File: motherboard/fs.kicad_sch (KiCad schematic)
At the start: 69 parts, among them J101 SC10L, J102 640389-2, Q101 MJD44H11, Q102 MJD45H11, U101 INA132UA, U102 LM741C, U103 LMH6609, U104 LM317, U105 LM337, U106 LM340-5, U107 MC7905ACD2T

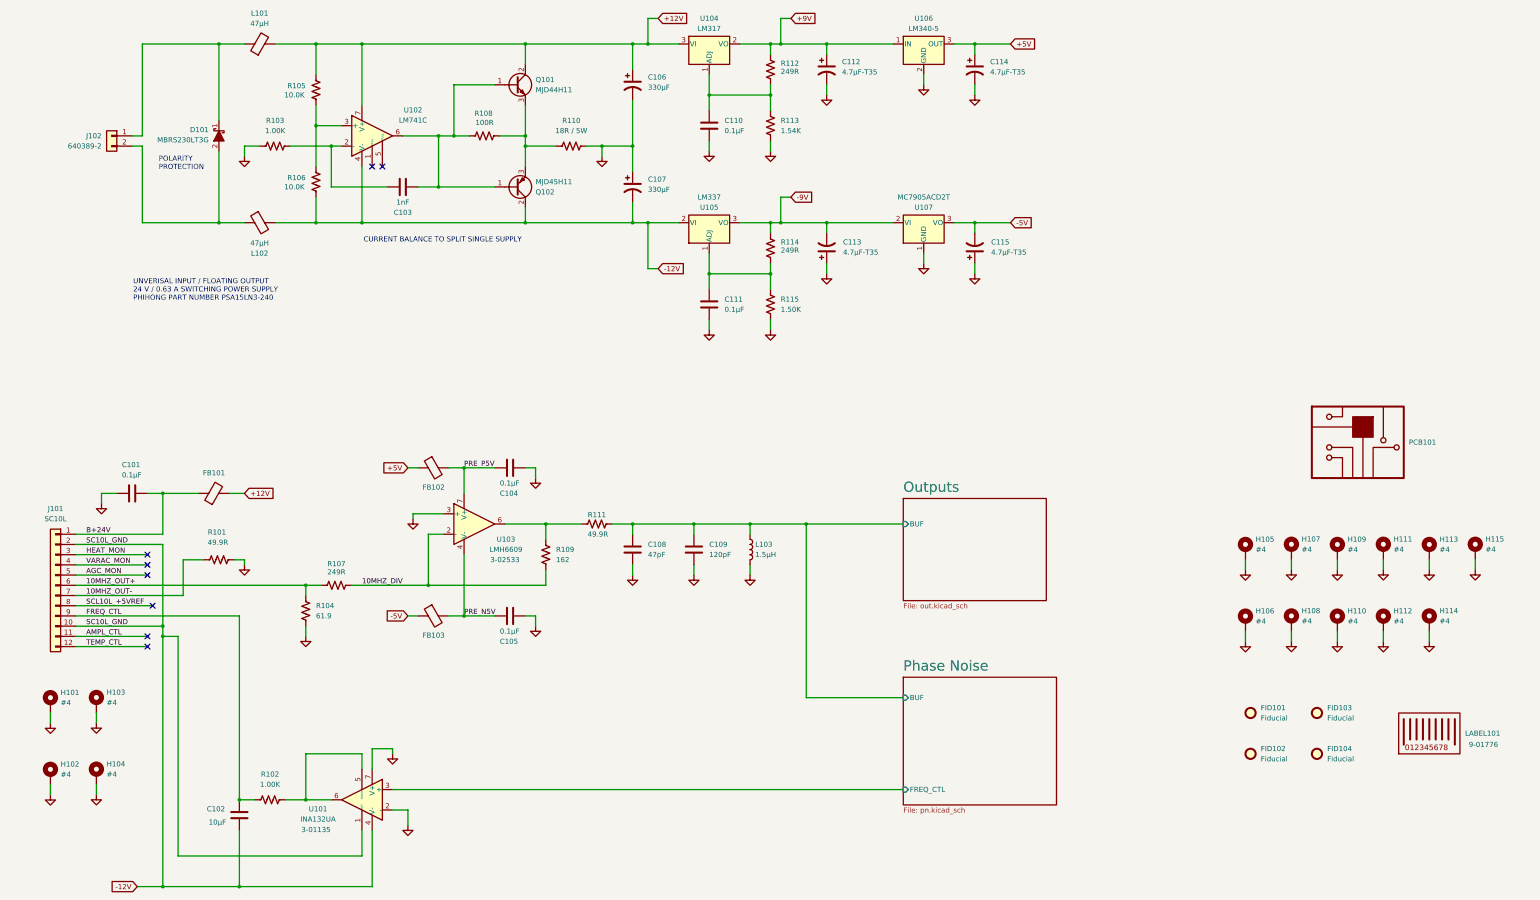
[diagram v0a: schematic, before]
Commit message: fix ERC issues
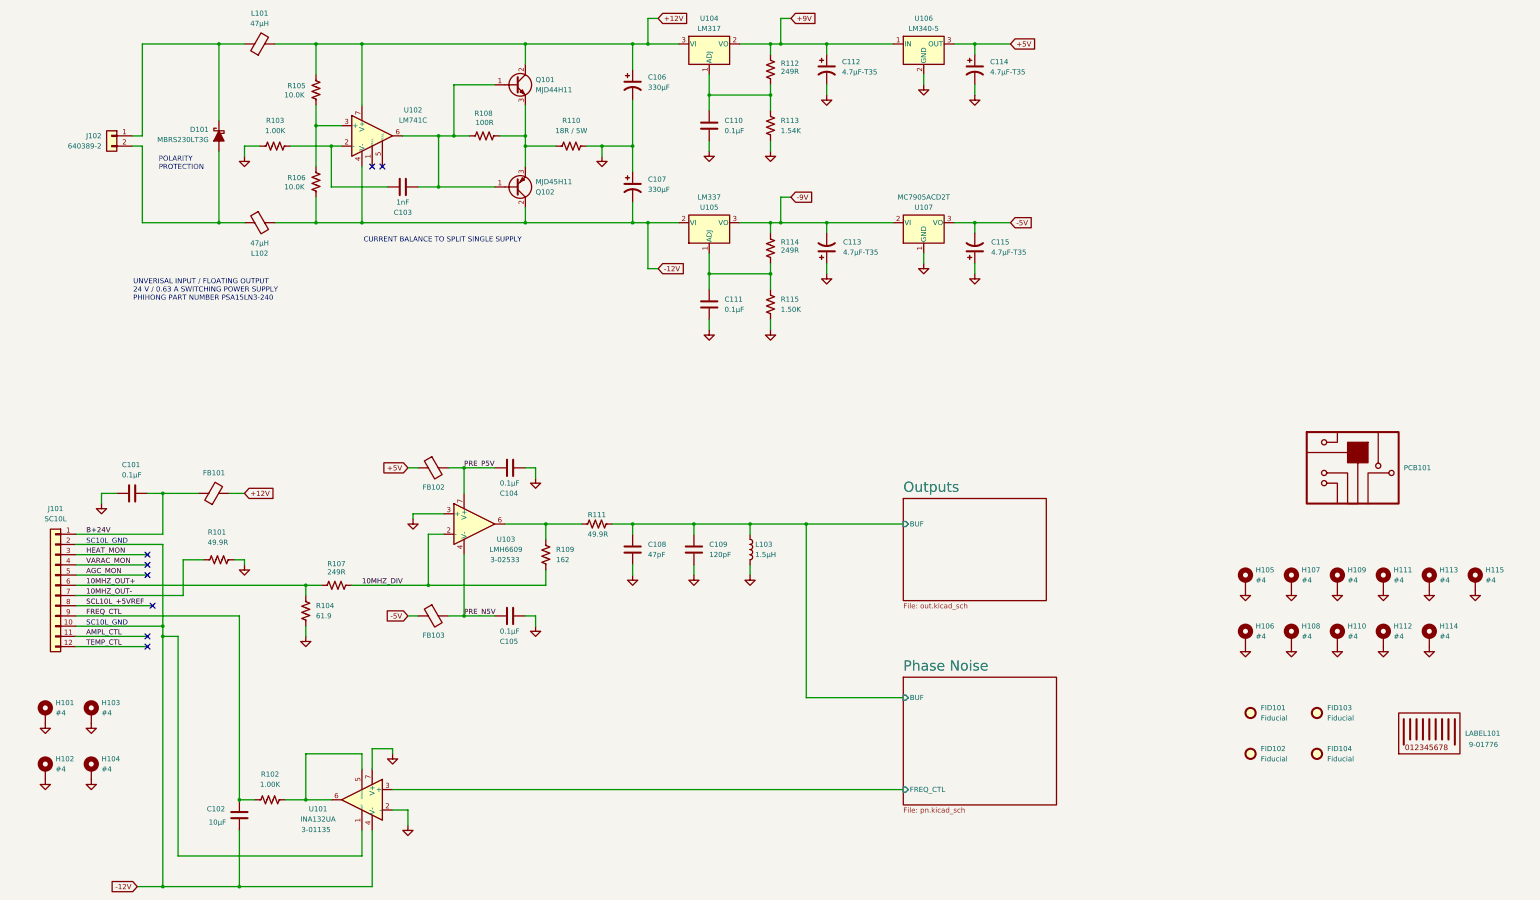
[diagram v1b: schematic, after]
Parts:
- removed D101: MBRS230LT3G, Diode_SMD:D_SMB, symbol SRS diodes:Schottky/MBRS230LT3G 2A 30V
- added D101: MBRS230LT3G, Diode_SMD:D_SMB, symbol #SRS:3_ICs/3-02091
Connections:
- net at J102.1 (Pin_1), L101.1: now also D101.1 (K)
- net at J102.2 (Pin_2), L102.1: now also D101.2 (A)
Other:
- note added: "SC10L_GND"
- moved on the sheet: H101, H102, H103, H104, H105, H106, H107, H108, H109, H110, H111, H112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

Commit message: add ESD protection (14V TVS)
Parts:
- C103: value 1nF -> 1nF NP0
- R104: value 61.9 -> 61.9R
- R109: value 162 -> 162R
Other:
- note added: "UNIVERSAL INPUT / FLOATING OUTPUT 24 V / 0.63 A SWITCHING POWER SUPPLY PHIHONG PART NUMBER PSA15LN3-240"
- note removed: "UNVERISAL INPUT / FLOATING OUTPUT 24 V / 0.63 A SWITCHING POWER SUPPLY PHIHONG PART NUMBER PSA15LN3-240"
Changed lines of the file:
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@@
 		)
 	)
-	(text "UNVERISAL INPUT / FLOATING OUTPUT\n24 V / 0.63 A SWITCHING POWER SUPPLY\nPHIHONG PART NUMBER PSA15LN3-240"
+	(text "UNIVERSAL INPUT / FLOATING OUTPUT\n24 V / 0.63 A SWITCHING POWER SUPPLY\nPHIHONG PART NUMBER PSA15LN3-240"
 		(exclude_from_sim no)
 		(at 57.404 100.584 0)
@@
 			)
 		)
-		(property "Value" "61.9"
+		(property "Value" "61.9R"
 			(at 102.87 181.6099 0)
 			(show_name no)
@@
 			)
 		)
-		(property "Value" "162"
+		(property "Value" "162R"
 			(at 162.56 167.6399 0)
 			(show_name no)
@@
 			)
 		)
-		(property "Value" "1nF"
+		(property "Value" "1nF NP0"
 			(at 124.46 78.74 90)
 			(show_name no)

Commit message: add mechanical parts to bom
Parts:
- J101: value SC10L -> Header; JLCPCB -- -> C7155422; MPN -- -> 1-215299-2; SRS PN -- -> 1-01602
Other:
- note added: "FEMALE HEADER TO SC10L ADAPTER BOARD"
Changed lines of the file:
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@@
 		)
 	)
+	(text "FEMALE HEADER TO SC10L\nADAPTER BOARD"
+		(exclude_from_sim no)
+		(at 40.64 194.564 0)
+		(effects
+			(font
+				(size 1.27 1.27)
+			)
+		)
+	)
 	(text "CURRENT BALANCE TO SPLIT SINGLE SUPPLY"
 		(exclude_from_sim no)
@@
 		(in_pos_files yes)
 		(dnp no)
-		(fields_autoplaced yes)
 		(property "Reference" "J101"
 			(at 38.1 154.94 0)
@@
 			)
 		)
-		(property "Value" "SC10L"
+		(property "Value" "Header"
 			(at 38.1 157.48 0)
+			(hide yes)
 			(show_name no)
 			(do_not_autoplace no)
@@
 			)
 		)
-		(property "JLCPCB" "--"
+		(property "JLCPCB" "C7155422"
 			(at 38.1 173.99 0)
 			(hide yes)
@@
 			)
 		)
-		(property "MPN" "--"
+		(property "MPN" "1-215299-2"
 			(at 38.1 173.99 0)
 			(hide yes)
@@
 			)
 		)
-		(property "SRS PN" "--"
-			(at 38.1 173.99 0)
-			(hide yes)
+		(property "SRS PN" "1-01602"
+			(at 38.1 157.988 0)
 			(show_name no)
 			(do_not_autoplace no)

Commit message: add schematic annotations
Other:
- note added: "ESTIMATED MAX CURRENT DRAW ========================== RAIL CURRENT POWER NOTES +12 V 0.52 A 6.24 W OCXO PLUS ALL POSITIVE-RAIL LOADS −12 V 0.52 A 6.24 W RETURN CURRENT OF THE FLOATING 24 V SUPPLY +9 V 0.31 A 2.79 W +5 V REG PLUS +9 V LOADS −9 V 0.24 A 2.16 W −5 V REG PLUS −9 V LOADS +5 V 0.21 A 1.05 W 8x LMH6609S PLUS SIX GROUNDED OUTPUTS −5 V 0.20 A 1.00 W 8x LMH6609S PLUS SIX GROUNDED OUTPUTS A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"
- note added: "UNIVERSAL INPUT / FLOATING OUTPUT 24 V / 1.50 A SWITCHING POWER SUPPLY MEANWELL PART NUMBER EPS-35-24"
- note removed: "UNIVERSAL INPUT / FLOATING OUTPUT 24 V / 0.63 A SWITCHING POWER SUPPLY PHIHONG PART NUMBER PSA15LN3-240"
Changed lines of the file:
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@@
+		)
+	)
+	(text "ESTIMATED MAX CURRENT DRAW\n==========================\n\nRAIL	CURRENT	POWER	NOTES\n+12 V	0.52 A	6.24 W	OCXO PLUS ALL POSITIVE-RAIL LOADS\n−12 V	0.52 A	6.24 W	RETURN CURRENT OF THE FLOATING 24 V SUPPLY\n+9 V	0.31 A	2.79 W	+5 V REG PLUS +9 V LOADS\n−9 V	0.24 A	2.16 W	−5 V REG PLUS −9 V LOADS\n+5 V	0.21 A	1.05 W	8x LMH6609S PLUS SIX GROUNDED OUTPUTS\n−5 V	0.20 A	1.00 W	8x LMH6609S PLUS SIX GROUNDED OUTPUTS\n\nASSUMPTIONS:\n\n	- SC-10L STABLE AT 25 °C\n	- ALL SIX OUTPUTS SHORTED TO GROUND"
+		(exclude_from_sim no)
+		(at 305.308 55.372 0)
+		(effects
+			(font
+				(size 1.27 1.27)
+			)
+			(justify left)
 		)
 	)
@@
 		)
 	)
-	(text "UNIVERSAL INPUT / FLOATING OUTPUT\n24 V / 0.63 A SWITCHING POWER SUPPLY\nPHIHONG PART NUMBER PSA15LN3-240"
+	(text "UNIVERSAL INPUT / FLOATING OUTPUT\n24 V / 1.50 A SWITCHING POWER SUPPLY\nMEANWELL PART NUMBER EPS-35-24"
 		(exclude_from_sim no)
-		(at 57.404 100.584 0)
+		(at 34.036 93.472 0)
 		(effects
 			(font

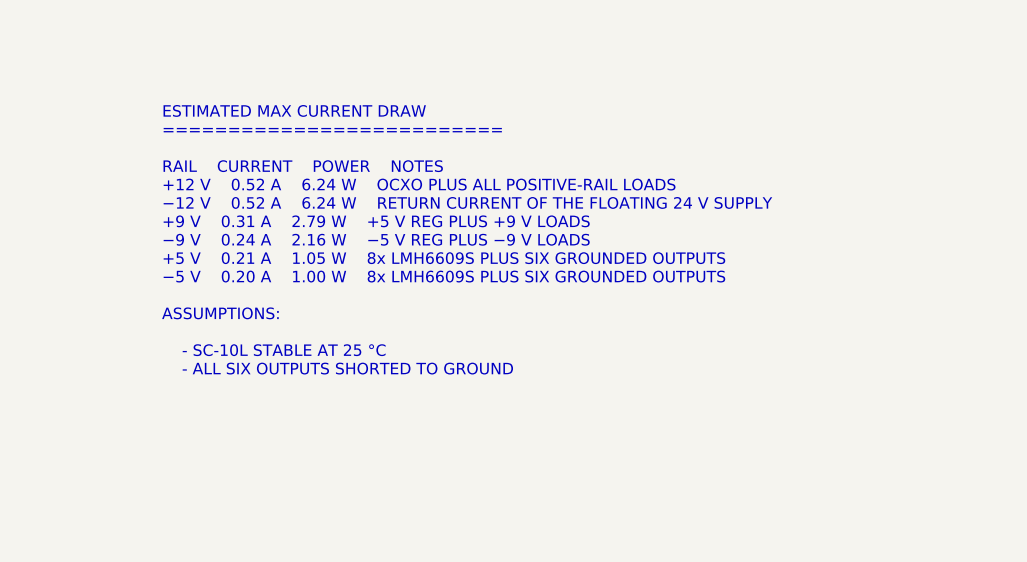
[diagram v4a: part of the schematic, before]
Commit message: update OCXO bead to SMB2.5R-2 (higher current)
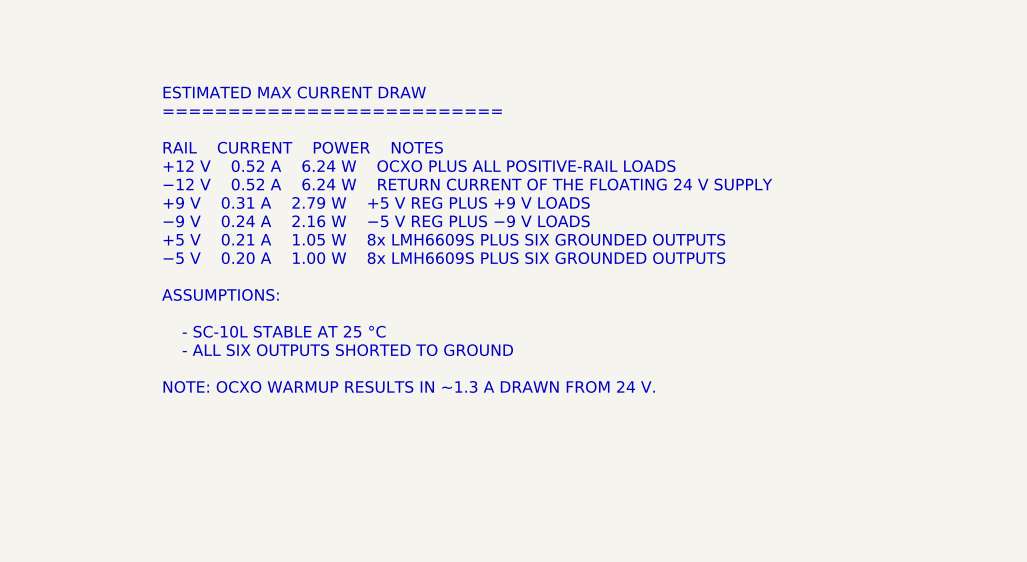
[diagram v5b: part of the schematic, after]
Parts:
- FB101: footprint Inductor_SMD:L_0603_1608Metric -> INDUCTOR_SRS:SMB2.5R-2; JLCPCB C2650942 -> C3716465; MPN 742863160 -> SMB2.5R-2; SRS PN 6-01344 -> 6-01322
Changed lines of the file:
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@@
 		)
 	)
-	(text "ESTIMATED MAX CURRENT DRAW\n==========================\n\nRAIL	CURRENT	POWER	NOTES\n+12 V	0.52 A	6.24 W	OCXO PLUS ALL POSITIVE-RAIL LOADS\n−12 V	0.52 A	6.24 W	RETURN CURRENT OF THE FLOATING 24 V SUPPLY\n+9 V	0.31 A	2.79 W	+5 V REG PLUS +9 V LOADS\n−9 V	0.24 A	2.16 W	−5 V REG PLUS −9 V LOADS\n+5 V	0.21 A	1.05 W	8x LMH6609S PLUS SIX GROUNDED OUTPUTS\n−5 V	0.20 A	1.00 W	8x LMH6609S PLUS SIX GROUNDED OUTPUTS\n\nASSUMPTIONS:\n\n	- SC-10L STABLE AT 25 °C\n	- ALL SIX OUTPUTS SHORTED TO GROUND"
+	(text "ESTIMATED MAX CURRENT DRAW\n==========================\n\nRAIL	CURRENT	POWER	NOTES\n+12 V	0.52 A	6.24 W	OCXO PLUS ALL POSITIVE-RAIL LOADS\n−12 V	0.52 A	6.24 W	RETURN CURRENT OF THE FLOATING 24 V SUPPLY\n+9 V	0.31 A	2.79 W	+5 V REG PLUS +9 V LOADS\n−9 V	0.24 A	2.16 W	−5 V REG PLUS −9 V LOADS\n+5 V	0.21 A	1.05 W	8x LMH6609S PLUS SIX GROUNDED OUTPUTS\n−5 V	0.20 A	1.00 W	8x LMH6609S PLUS SIX GROUNDED OUTPUTS\n\nASSUMPTIONS:\n\n	- SC-10L STABLE AT 25 °C\n	- ALL SIX OUTPUTS SHORTED TO GROUND\n\nNOTE: OCXO WARMUP RESULTS IN ~1.3 A DRAWN FROM 24 V."
 		(exclude_from_sim no)
 		(at 305.308 55.372 0)
@@
 			)
 		)
-		(property "Footprint" "Inductor_SMD:L_0603_1608Metric"
+		(property "Footprint" "INDUCTOR_SRS:SMB2.5R-2"
 			(at 77.47 152.908 90)
 			(hide yes)
@@
 			)
 		)
-		(property "Description" "0603 Ferrite bead, 400 mA"
+		(property "Description" "Ferrite bead,SMB, 9500 mA, 490 ohms@100 MHz, 0.005 ohm@DC, SMB2.5R-2"
 			(at 77.47 151.13 0)
 			(hide yes)
@@
 			)
 		)
-		(property "SRS PN" "6-01344"
+		(property "SRS PN" "6-01322"
 			(at 77.47 151.13 0)
 			(hide yes)
@@
 			)
 		)
-		(property "JLCPCB" "C2650942"
+		(property "JLCPCB" "C3716465"
 			(at 77.47 151.13 0)
 			(hide yes)
@@
 			)
 		)
-		(property "MPN" "742863160"
+		(property "MPN" "SMB2.5R-2"
 			(at 77.47 151.13 90)
 			(hide yes)

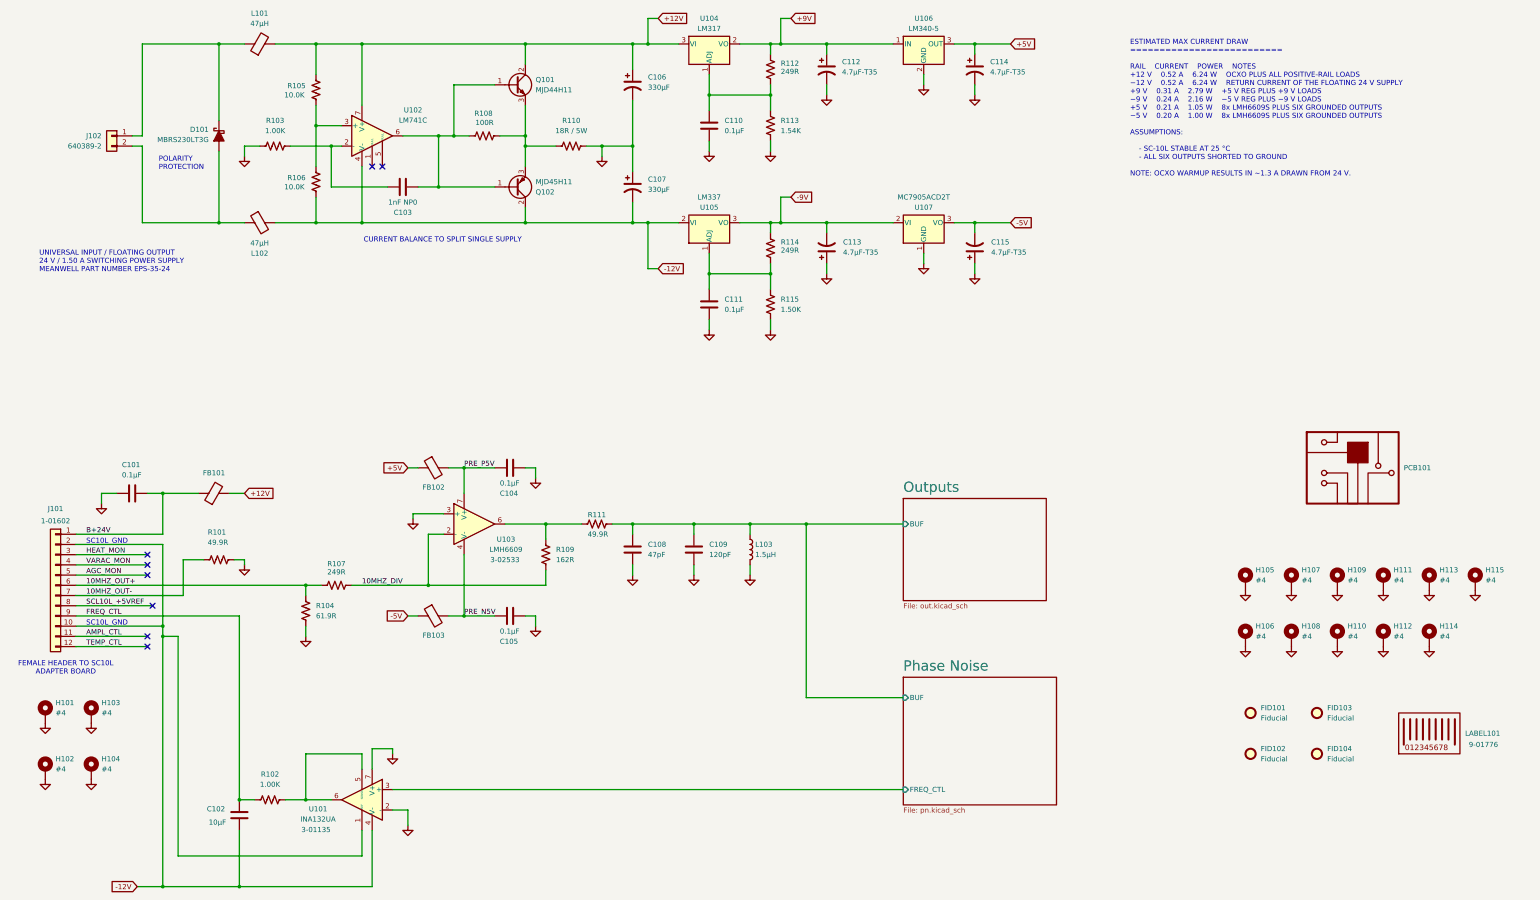
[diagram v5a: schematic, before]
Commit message: add testpoints
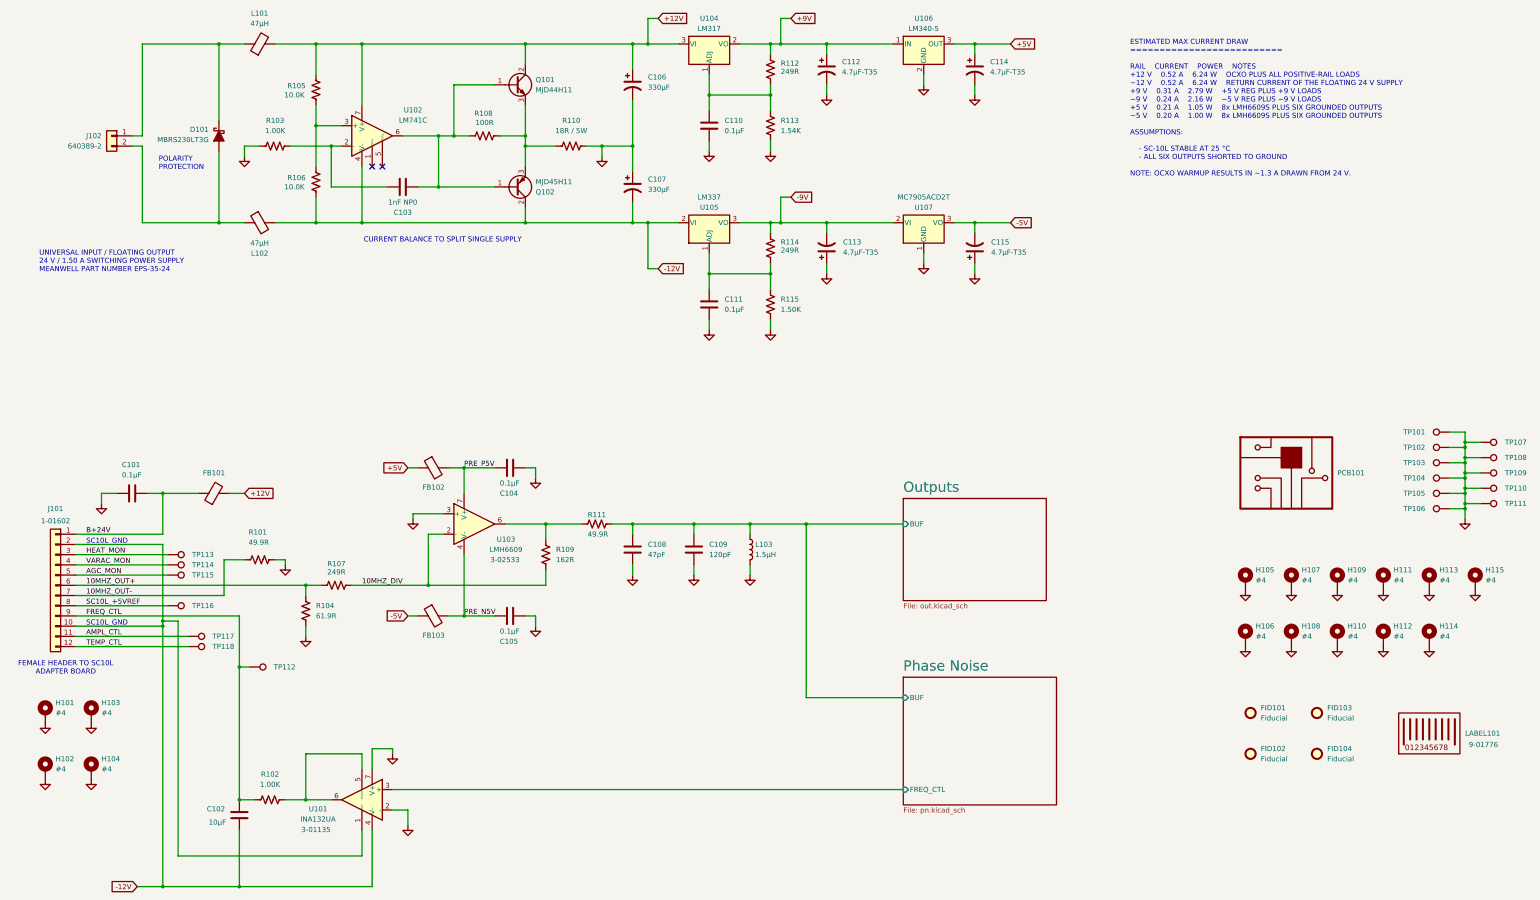
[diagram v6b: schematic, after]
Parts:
- added TP101, TP102, TP103, TP104, TP105, TP106, TP107, TP108, TP109, TP110, TP111: TestPoint, TestPoint:TestPoint_THTPad_D2.0mm_Drill1.0mm, symbol Connector:TestPoint
- added TP112, TP113, TP114, TP115, TP116, TP117, TP118: TestPoint, TestPoint:TestPoint_THTPad_D1.0mm_Drill0.5mm, symbol Connector:TestPoint
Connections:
- net AGC_MON: now also TP115.1
- net AMPL_CTL: now also TP117.1
- net FREQ_CTL: now also TP112.1
- net GND: now also TP101.1, TP102.1, TP103.1, TP104.1, TP105.1, TP106.1, TP107.1, TP108.1, TP109.1, TP110.1, TP111.1
- net HEAT_MON: now also TP113.1
- net TEMP_CTL: now also TP118.1
- net VARAC_MON: now also TP114.1
- net SCL10L_+5VREF renamed SC10L_+5VREF
- net SC10L_+5VREF: now also TP116.1
- no-connect marks 8 -> 2
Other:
- moved on the sheet: PCB101, R101
